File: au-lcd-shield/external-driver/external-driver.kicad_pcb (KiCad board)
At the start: 2 copper layers, 65 x 45 mm, 6 parts, among them IC2 DSLVDS1047PWR, J1 Power, J2 Backlight, J4 Conn_02x09_Odd_Even, U1 UA78M33CDCYR

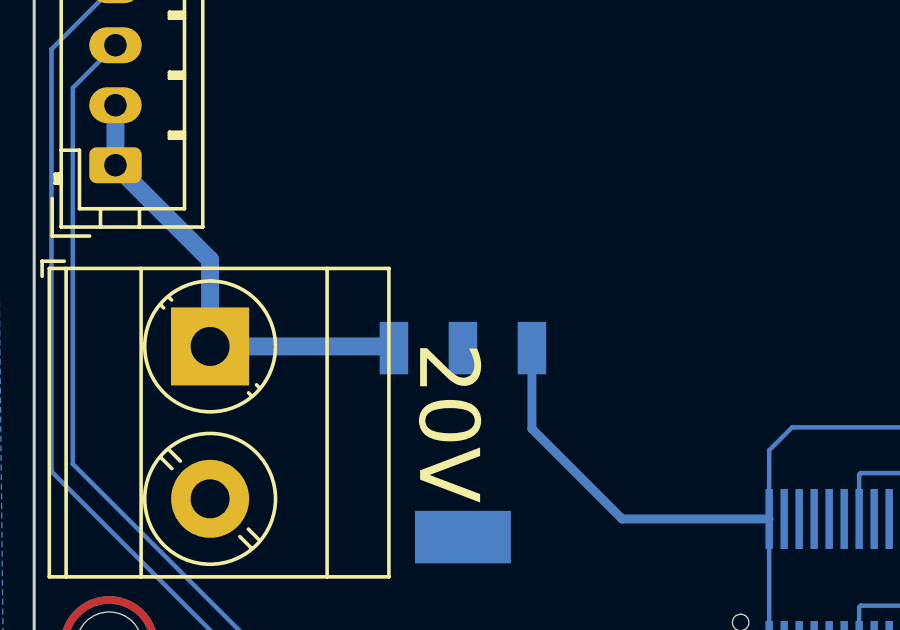
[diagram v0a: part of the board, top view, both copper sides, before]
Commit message: add filtering caps for ldo's
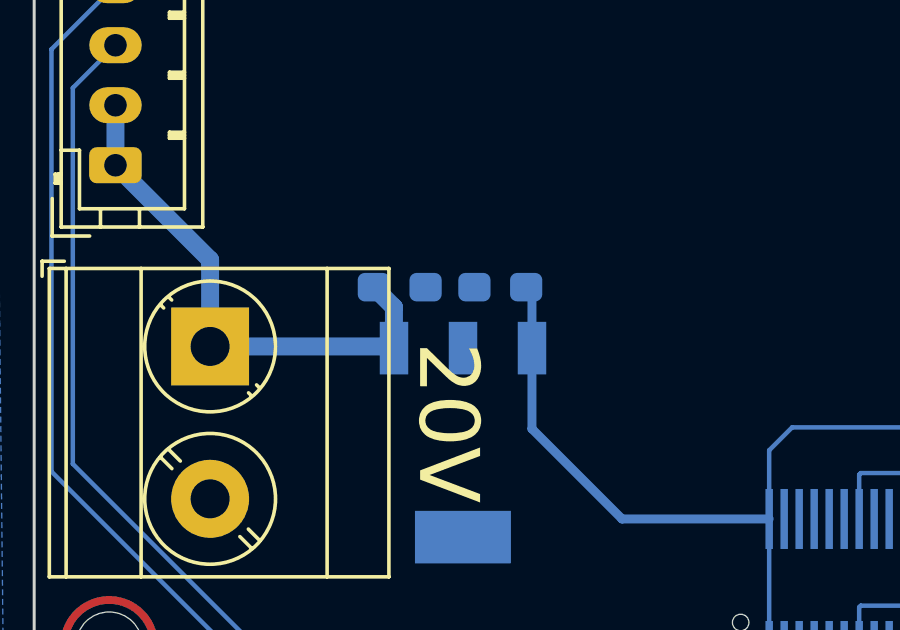
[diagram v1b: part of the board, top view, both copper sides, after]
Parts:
- added C1: 10uF, Capacitor_SMD:C_0603_1608Metric_Pad1.08x0.95mm_HandSolder, B.Cu at (123.6, 108.1)
- added C2: 10uF, Capacitor_SMD:C_0603_1608Metric_Pad1.08x0.95mm_HandSolder, B.Cu at (127.0, 108.1)
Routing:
- net VCC: track 15.5 -> 17.8 mm
- net +5V: track 42.7 -> 44.8 mm
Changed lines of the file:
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@@
+    )
+  )
+  (footprint "Capacitor_SMD:C_0603_1608Metric_Pad1.08x0.95mm_HandSolder" (layer "B.Cu")
+    (at 126.9746 108.1024)
+    (descr "Capacitor SMD 0603 (1608 Metric), square (rectangular) end terminal, IPC_7351 nominal with elongated pad for handsoldering. (Body size source: IPC-SM-782 page 76, https://www.pcb-3d.com/wordpress/wp-content/uploads/ipc-sm-782a_amendment_1_and_2.pdf), generated with kicad-footprint-generator")
+    (tags "capacitor handsolder")
+    (property "Sheetfile" "external-driver.kicad_sch")
+    (property "Sheetname" "")
+    (property "ki_description" "Unpolarized capacitor")
+    (property "ki_keywords" "cap capacitor")
+    (attr smd)
+    (fp_text reference "C2" (at 0 1.43) (layer "B.SilkS") hide
+        (effects (font (size 1 1) (thickness 0.15)) (justify mirror))
+    )
+    (fp_text value "10uF" (at 0 -1.43) (layer "B.Fab")
+        (effects (font (size 1 1) (thickness 0.15)) (justify mirror))
+    )
+    (fp_text user "${REFERENCE}" (at 0 0) (layer "B.Fab")
+        (effects (font (size 0.4 0.4) (thickness 0.06)) (justify mirror))
+    )
+    (fp_line (start -0.146267 -0.51) (end 0.146267 -0.51)
+      (stroke (width 0.12) (type solid)) (layer "B.SilkS"))
+    (fp_line (start -0.146267 0.51) (end 0.146267 0.51)
+      (stroke (width 0.12) (type solid)) (layer "B.SilkS"))
+    (fp_line (start -1.65 -0.73) (end -1.65 0.73)
+      (stroke (width 0.05) (type solid)) (layer "B.CrtYd"))
+    (fp_line (start -1.65 0.73) (end 1.65 0.73)
+      (stroke (width 0.05) (type solid)) (layer "B.CrtYd"))
+    (fp_line (start 1.65 -0.73) (end -1.65 -0.73)
+      (stroke (width 0.05) (type solid)) (layer "B.CrtYd"))
+    (fp_line (start 1.65 0.73) (end 1.65 -0.73)
+      (stroke (width 0.05) (type solid)) (layer "B.CrtYd"))
+    (fp_line (start -0.8 -0.4) (end -0.8 0.4)
+      (stroke (width 0.1) (type solid)) (layer "B.Fab"))
+    (fp_line (start -0.8 0.4) (end 0.8 0.4)
+      (stroke (width 0.1) (type solid)) (layer "B.Fab"))
+    (fp_line (start 0.8 -0.4) (end -0.8 -0.4)
+      (stroke (width 0.1) (type solid)) (layer "B.Fab"))
+    (fp_line (start 0.8 0.4) (end 0.8 -0.4)
+      (stroke (width 0.1) (type solid)) (layer "B.Fab"))
+    (pad "1" smd roundrect (at -0.8625 0) (size 1.075 0.95) (layers "B.Cu" "B.Paste" "B.Mask") (roundrect_rratio 0.25)
+      (net 1 "GND") (pintype "passive"))
+    (pad "2" smd roundrect (at 0.8625 0) (size 1.075 0.95) (layers "B.Cu" "B.Paste" "B.Mask") (roundrect_rratio 0.25)
+      (net 134 "+5V") (pintype "passive"))
+    (model "${KICAD6_3DMODEL_DIR}/Capacitor_SMD.3dshapes/C_0603_1608Metric.wrl"
+      (offset (xyz 0 0 0))
+      (scale (xyz 1 1 1))
+      (rotate (xyz 0 0 0))
     )
   )
@@
     )
   )
+  (footprint "Capacitor_SMD:C_0603_1608Metric_Pad1.08x0.95mm_HandSolder" (layer "B.Cu")
+    (at 123.6218 108.1024 180)
+    (descr "Capacitor SMD 0603 (1608 Metric), square (rectangular) end terminal, IPC_7351 nominal with elongated pad for handsoldering. (Body size source: IPC-SM-782 page 76, https://www.pcb-3d.com/wordpress/wp-content/uploads/ipc-sm-782a_amendment_1_and_2.pdf), generated with kicad-footprint-generator")
+    (tags "capacitor handsolder")
+    (property "Sheetfile" "external-driver.kicad_sch")
+    (property "Sheetname" "")
+    (property "ki_description" "Unpolarized capacitor")
+    (property "ki_keywords" "cap capacitor")
+    (attr smd)
+    (fp_text reference "C1" (at 0 1.43) (layer "B.SilkS") hide
+        (effects (font (size 1 1) (thickness 0.15)) (justify mirror))
+    )
+    (fp_text value "10uF" (at 0 -1.43) (layer "B.Fab")
+        (effects (font (size 1 1) (thickness 0.15)) (justify mirror))
+    )
+    (fp_text user "${REFERENCE}" (at 0 0) (layer "B.Fab")
+        (effects (font (size 0.4 0.4) (thickness 0.06)) (justify mirror))
+    )
+    (fp_line (start -0.146267 -0.51) (end 0.146267 -0.51)
+      (stroke (width 0.12) (type solid)) (layer "B.SilkS"))
+    (fp_line (start -0.146267 0.51) (end 0.146267 0.51)
+      (stroke (width 0.12) (type solid)) (layer "B.SilkS"))
+    (fp_line (start -1.65 -0.73) (end -1.65 0.73)
+      (stroke (width 0.05) (type solid)) (layer "B.CrtYd"))
+    (fp_line (start -1.65 0.73) (end 1.65 0.73)
+      (stroke (width 0.05) (type solid)) (layer "B.CrtYd"))
+    (fp_line (start 1.65 -0.73) (end -1.65 -0.73)
+      (stroke (width 0.05) (type solid)) (layer "B.CrtYd"))
+    (fp_line (start 1.65 0.73) (end 1.65 -0.73)
+      (stroke (width 0.05) (type solid)) (layer "B.CrtYd"))
+    (fp_line (start -0.8 -0.4) (end -0.8 0.4)
+      (stroke (width 0.1) (type solid)) (layer "B.Fab"))
+    (fp_line (start -0.8 0.4) (end 0.8 0.4)
+      (stroke (width 0.1) (type solid)) (layer "B.Fab"))
+    (fp_line (start 0.8 -0.4) (end -0.8 -0.4)
+      (stroke (width 0.1) (type solid)) (layer "B.Fab"))
+    (fp_line (start 0.8 0.4) (end 0.8 -0.4)
+      (stroke (width 0.1) (type solid)) (layer "B.Fab"))
+    (pad "1" smd roundrect (at -0.8625 0 180) (size 1.075 0.95) (layers "B.Cu" "B.Paste" "B.Mask") (roundrect_rratio 0.25)
+      (net 1 "GND") (pintype "passive"))
+    (pad "2" smd roundrect (at 0.8625 0 180) (size 1.075 0.95) (layers "B.Cu" "B.Paste" "B.Mask") (roundrect_rratio 0.25)
+      (net 15 "VCC") (pintype "passive"))
+    (model "${KICAD6_3DMODEL_DIR}/Capacitor_SMD.3dshapes/C_0603_1608Metric.wrl"
+      (offset (xyz 0 0 0))
+      (scale (xyz 1 1 1))
+      (rotate (xyz 0 0 0))
+    )
+  )
   (footprint "SamacSys_Parts:SOT230P700X180-4N" (layer "B.Cu")
     (at 125.73 113.284 -90)
@@
         (effects (font (size 1.27 1.27) (thickness 0.254)) (justify mirror))
     )
-    (fp_text user "5V" (at -4.9276 -0.1016 unlocked) (layer "B.SilkS")
+    (fp_text user "5V" (at -2.7432 -4.699 unlocked) (layer "B.SilkS")
         (effects (font (size 1 1) (thickness 0.15)) (justify mirror))
     )
@@
   (segment (start 117.302 110.0786) (end 123.3746 110.0786) (width 0.6) (layer "B.Cu") (net 15))
   (segment (start 114.1476 102.0384) (end 114.1476 104.0384) (width 0.6) (layer "B.Cu") (net 15))
+  (segment (start 123.43 108.7731) (end 122.7593 108.1024) (width 0.6) (layer "B.Cu") (net 15))
   (segment (start 123.3746 110.0786) (end 123.43 110.134) (width 0.6) (layer "B.Cu") (net 15))
+  (segment (start 123.43 110.134) (end 123.43 108.7731) (width 0.6) (layer "B.Cu") (net 15))
   (segment (start 117.302 107.1928) (end 117.302 110.0786) (width 0.6) (layer "B.Cu") (net 15))
   (segment (start 114.1476 104.0384) (end 117.302 107.1928) (width 0.6) (layer "B.Cu") (net 15))
@@
   (segment (start 131.0336 115.83) (end 135.9375 115.83) (width 0.3) (layer "B.Cu") (net 134))
   (segment (start 157.4375 113.9527) (end 157.4375 115.83) (width 0.15) (layer "B.Cu") (net 134))
+  (segment (start 128.03 110.134) (end 128.03 108.2953) (width 0.3) (layer "B.Cu") (net 134))
+  (segment (start 128.03 108.2953) (end 127.8371 108.1024) (width 0.3) (layer "B.Cu") (net 134))
   (zone (net 1) (net_name "GND") (layer "B.Cu") (hatch edge 0.5)
     (connect_pads (clearance 0.25))

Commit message: pcb v1.0
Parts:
- U1: value UA78M33CDCYR -> 78M05; footprint SamacSys_Parts:SOT230P700X180-4N -> Package_TO_SOT_SMD:TO-252-2
- moved U1 2.00 mm to (125.6, 115.3)
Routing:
- net +5V: track 44.8 -> 74.3 mm
- net GND: vias 0 -> 253
- added copper zone on F.Cu, net GND
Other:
- board text added: "+"
- board text added: "-"
- board text added: "{ "ViaStitching": "0.2", "stitch_zone_0": { "HSpacing": "1", "VSpacing": "1", "Clearance": "1", "Randomize": false } }"

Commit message: fix pins WIP
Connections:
- B1 pad B_12: unconnected-(B1B-F4-PadB_12) -> TX1_B_IN
- B1 pad B_2: TXCLK_B_IN -> unconnected-(B1B-D1-PadB_2)
- B1 pad B_5: TX1_B_IN -> unconnected-(B1B-A2-PadB_5)
- B1 pad B_9: unconnected-(B1B-F2-PadB_9) -> TXCLK_B_IN
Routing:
- net TX1_B_IN: track 3.02 -> 1.40 mm
- net TXCLK_B_IN: track 3.24 -> 2.17 mm
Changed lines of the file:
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@@
   (net 5 "TX2_B_IN")
   (net 6 "TXCLK_B_IN")
-  (net 7 "unconnected-(B1B-F2-PadB_9)")
+  (net 7 "unconnected-(B1B-D1-PadB_2)")
   (net 8 "unconnected-(B1B-E1-PadB_8)")
   (net 9 "TXCLK_P")
@@
   (net 41 "unconnected-(B1A-T10-PadA_49)")
   (net 42 "unconnected-(B1B-F3-PadB_11)")
-  (net 43 "unconnected-(B1B-F4-PadB_12)")
+  (net 43 "unconnected-(B1B-A2-PadB_5)")
   (net 44 "unconnected-(B1B-A3-PadB_14)")
   (net 45 "unconnected-(B1B-B4-PadB_15)")
@@
       (net 134 "+5V") (pinfunction "5V") (pintype "passive") (solder_mask_margin 0.102))
     (pad "B_2" smd rect locked (at 46.5 -38.3 90) (size 2 0.25) (layers "B.Cu" "B.Paste" "B.Mask")
-      (net 6 "TXCLK_B_IN") (pinfunction "D1") (pintype "passive") (solder_mask_margin 0.102))
+      (net 7 "unconnected-(B1B-D1-PadB_2)") (pinfunction "D1") (pintype "passive") (solder_mask_margin 0.102))
     (pad "B_3" smd rect locked (at 47 -38.3 90) (size 2 0.25) (layers "B.Cu" "B.Paste" "B.Mask")
       (net 5 "TX2_B_IN") (pinfunction "E2") (pintype "passive") (solder_mask_margin 0.102))
@@
       (net 1 "GND") (pinfunction "GND") (pintype "passive") (solder_mask_margin 0.102))
     (pad "B_5" smd rect locked (at 48 -38.3 90) (size 2 0.25) (layers "B.Cu" "B.Paste" "B.Mask")
-      (net 4 "TX1_B_IN") (pinfunction "A2") (pintype "passive") (solder_mask_margin 0.102))
+      (net 43 "unconnected-(B1B-A2-PadB_5)") (pinfunction "A2") (pintype "passive") (solder_mask_margin 0.102))
     (pad "B_6" smd rect locked (at 48.5 -38.3 90) (size 2 0.25) (layers "B.Cu" "B.Paste" "B.Mask")
-      (net 3 "TX0_B_IN") (pinfunction "E2") (pintype "passive") (solder_mask_margin 0.102))
+      (net 3 "TX0_B_IN") (pinfunction "B2") (pintype "passive") (solder_mask_margin 0.102))
     (pad "B_7" smd rect locked (at 49 -38.3 90) (size 2 0.25) (layers "B.Cu" "B.Paste" "B.Mask")
       (net 2 "+3.3V") (pinfunction "3V3") (pintype "passive") (solder_mask_margin 0.102))
@@
       (net 8 "unconnected-(B1B-E1-PadB_8)") (pinfunction "E1") (pintype "passive") (solder_mask_margin 0.102))
     (pad "B_9" smd rect locked (at 50 -38.3 90) (size 2 0.25) (layers "B.Cu" "B.Paste" "B.Mask")
-      (net 7 "unconnected-(B1B-F2-PadB_9)") (pinfunction "F2") (pintype "passive") (solder_mask_margin 0.102))
+      (net 6 "TXCLK_B_IN") (pinfunction "F2") (pintype "passive") (solder_mask_margin 0.102))
     (pad "B_10" smd rect locked (at 50.5 -38.3 90) (size 2 0.25) (layers "B.Cu" "B.Paste" "B.Mask")
       (net 1 "GND") (pinfunction "GND") (pintype "passive") (solder_mask_margin 0.102))
@@
       (net 42 "unconnected-(B1B-F3-PadB_11)") (pinfunction "F3") (pintype "passive") (solder_mask_margin 0.102))
     (pad "B_12" smd rect locked (at 51.5 -38.3 90) (size 2 0.25) (layers "B.Cu" "B.Paste" "B.Mask")
-      (net 43 "unconnected-(B1B-F4-PadB_12)") (pinfunction "F4") (pintype "passive") (solder_mask_margin 0.102))
+      (net 4 "TX1_B_IN") (pinfunction "F4") (pintype "passive") (solder_mask_margin 0.102))
     (pad "B_13" smd rect locked (at 52 -38.3 90) (size 2 0.25) (layers "B.Cu" "B.Paste" "B.Mask")
       (net 2 "+3.3V") (pinfunction "3V3") (pintype "passive") (solder_mask_margin 0.102))
@@
       (stroke (width 0.1) (type solid)) (layer "B.Fab"))
     (pad "1" smd rect (at -2.938 2.275 180) (size 0.45 1.475) (layers "B.Cu" "B.Paste" "B.Mask")
-      (net 136 "unconnected-(IC2-EN_1-Pad1)") (pinfunction "EN_1") (pintype "passive"))
+      (net 136 "unconnected-(IC2-EN_1-Pad1)") (pinfunction "EN_1") (pintype "passive+no_connect"))
     (pad "2" smd rect (at -2.938 1.625 180) (size 0.45 1.475) (layers "B.Cu" "B.Paste" "B.Mask")
       (net 6 "TXCLK_B_IN") (pinfunction "DIN1") (pintype "passive"))
@@
       (net 3 "TX0_B_IN") (pinfunction "DIN4") (pintype "passive"))
     (pad "8" smd rect (at -2.938 -2.275 180) (size 0.45 1.475) (layers "B.Cu" "B.Paste" "B.Mask")
-      (net 137 "unconnected-(IC2-EN_2-Pad8)") (pinfunction "EN_2") (pintype "passive"))
+      (net 137 "unconnected-(IC2-EN_2-Pad8)") (pinfunction "EN_2") (pintype "passive+no_connect"))
     (pad "9" smd rect (at 2.938 -2.275 180) (size 0.45 1.475) (layers "B.Cu" "B.Paste" "B.Mask")
       (net 17 "TX0_N") (pinfunction "DOUT4-") (pintype "passive"))
@@
   (segment (start 160.375 87.1304) (end 160.375 85.610698) (width 0.15) (layer "B.Cu") (net 3))
   (segment (start 159.725 87.1304) (end 159.725 86.1412) (width 0.15) (layer "B.Cu") (net 4))
-  (segment (start 159.4375 85.8537) (end 159.4375 84.23) (width 0.15) (layer "B.Cu") (net 4))
   (segment (start 159.725 86.1412) (end 159.4375 85.8537) (width 0.15) (layer "B.Cu") (net 4))
   (segment (start 157.775 86.3952) (end 158.4375 85.7327) (width 0.15) (layer "B.Cu") (net 5))
   (segment (start 157.775 87.1304) (end 157.775 86.3952) (width 0.15) (layer "B.Cu") (net 5))
   (segment (start 158.4375 85.7327) (end 158.4375 84.23) (width 0.15) (layer "B.Cu") (net 5))
-  (segment (start 157.9375 85.2929) (end 157.9375 84.23) (width 0.15) (layer "B.Cu") (net 6))
   (segment (start 157.125 86.1054) (end 157.9375 85.2929) (width 0.15) (layer "B.Cu") (net 6))
   (segment (start 157.125 87.1304) (end 157.125 86.1054) (width 0.15) (layer "B.Cu") (net 6))
